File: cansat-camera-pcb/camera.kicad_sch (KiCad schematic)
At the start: 22 parts, among them IC1 TLV74315PDBVR, J3 OV5640, U1 TLV74328PDBVR

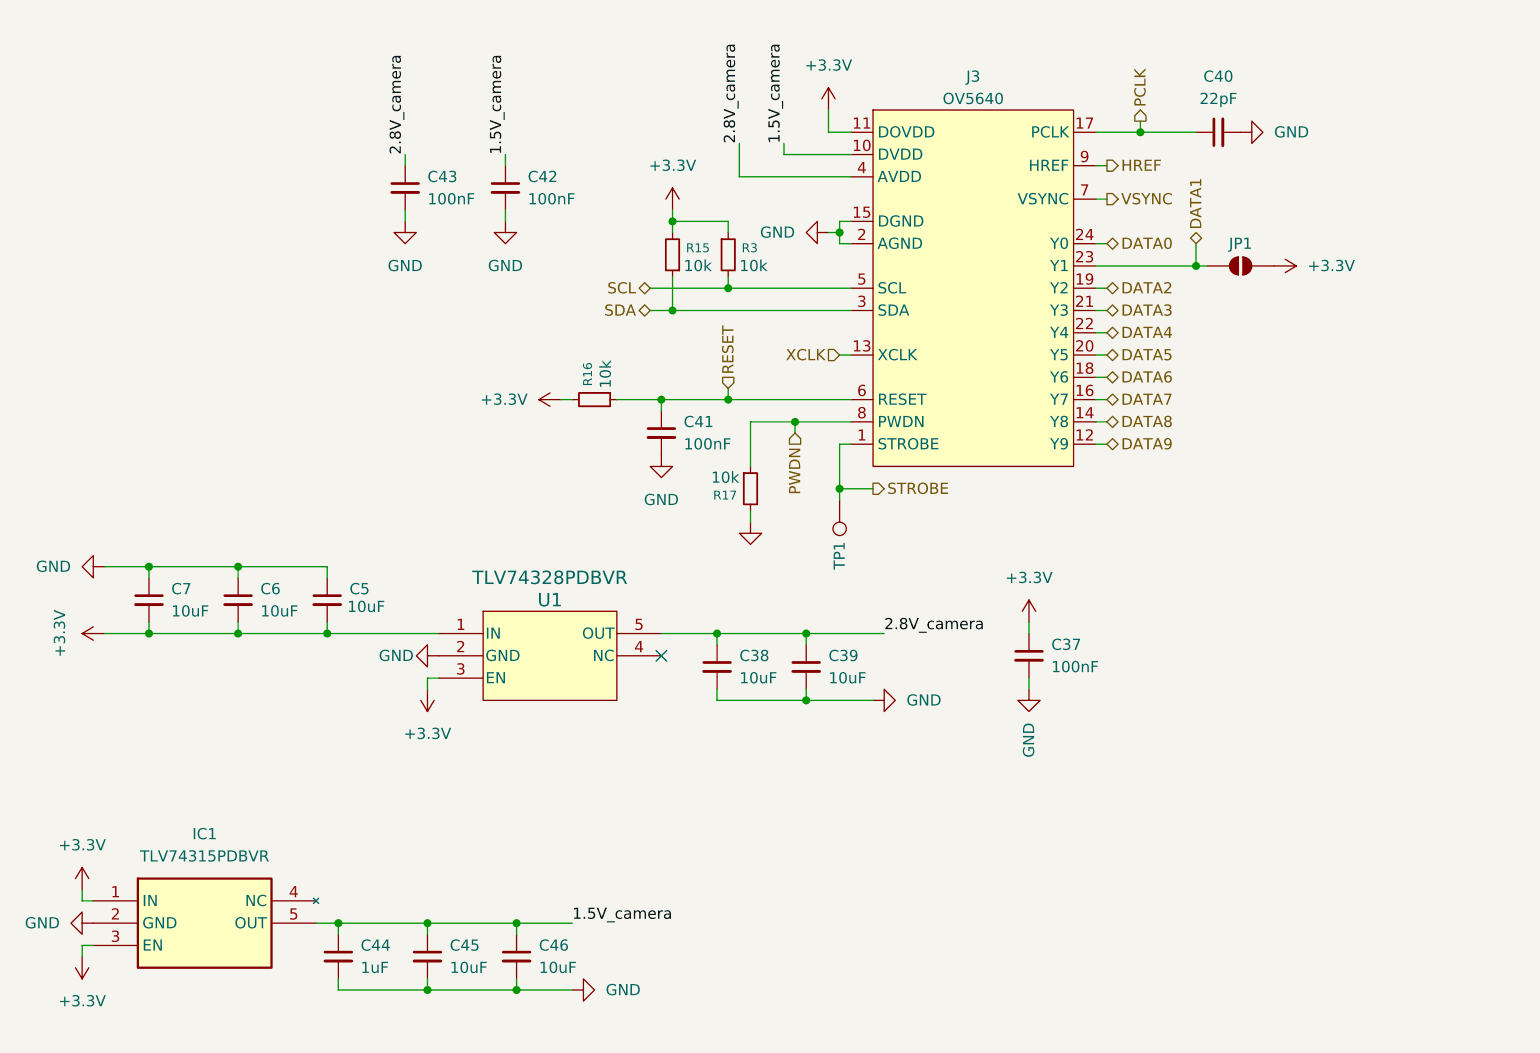
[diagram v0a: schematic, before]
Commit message: -4g modul(4g modul on other pcb)
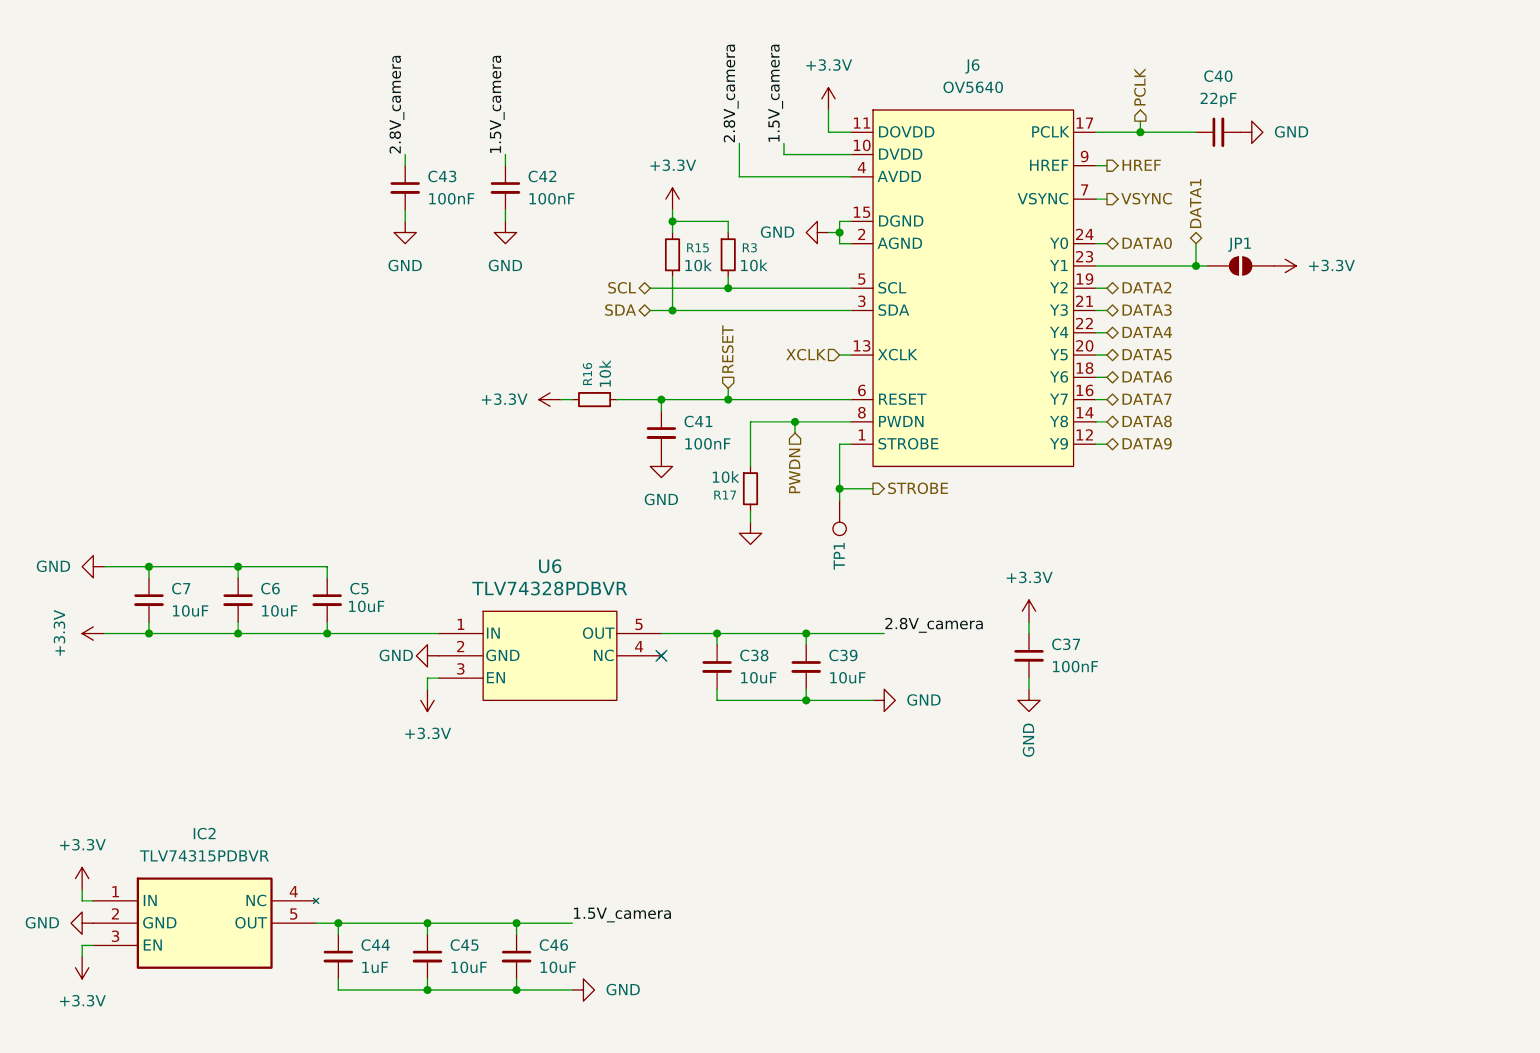
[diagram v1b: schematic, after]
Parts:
- removed IC1: TLV74315PDBVR, SOT95P280X145-5N, symbol cansat-camera-pcb-symbols:TLV74315PDBVR
- removed J3: OV5640, symbol cansat-camera-pcb-symbols:OV2640
- removed U1: TLV74328PDBVR, DBV0005A_N, symbol cansat-camera-pcb-symbols:TLV74328PDBVR
- added IC2: TLV74315PDBVR, SOT95P280X145-5N, symbol gaia-camera-symbols:TLV74315PDBVR
- added J6: OV5640, symbol gaia-camera-symbols:OV2640
- added U6: TLV74328PDBVR, DBV0005A_N, symbol gaia-camera-symbols:TLV74328PDBVR
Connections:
- net +3.3V: now also IC2.1 (IN), IC2.3 (EN), J6.11 (DOVDD), U6.1 (IN), U6.3 (EN)
- net 1.5V_camera: now also IC2.5 (OUT), J6.10 (DVDD)
- net 2.8V_camera: now also J6.4 (AVDD), U6.5 (OUT)
- net DATA0: now also J6.24 (Y0)
- net DATA1: now also J6.23 (Y1)
- net DATA2: now also J6.19 (Y2)
- net DATA3: now also J6.21 (Y3)
- net DATA4: now also J6.22 (Y4)
- net DATA5: now also J6.20 (Y5)
- net DATA6: now also J6.18 (Y6)
- net DATA7: now also J6.16 (Y7)
- net DATA8: now also J6.14 (Y8)
- net DATA9: now also J6.12 (Y9)
- net GND: now also IC2.2 (GND), J6.15 (DGND), J6.2 (AGND), U6.2 (GND)
- net HREF: now also J6.9 (HREF)
- net PCLK: now also J6.17 (PCLK)
- net PWDN: now also J6.8 (PWDN)
- net RESET: now also J6.6 (RESET)
- net SCL: now also J6.5 (SCL)
- net SDA: now also J6.3 (SDA)
- net STROBE: now also J6.1 (STROBE)
- net VSYNC: now also J6.7 (VSYNC)
- net XCLK: now also J6.13 (XCLK)

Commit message: -
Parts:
- IC2: footprint SOT95P280X145-5N -> gaia-camera-footprints:TLV74315PDBVR
- U6: footprint DBV0005A_N -> gaia-camera-footprints:TLV74328PDBVR
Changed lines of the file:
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@@
 			)
 		)
-		(property "Footprint" "SOT95P280X145-5N"
+		(property "Footprint" "gaia-camera-footprints:TLV74315PDBVR"
 			(at 43.18 213.03 0)
 			(effects
@@
 			)
 		)
-		(property "Footprint" "DBV0005A_N"
+		(property "Footprint" "gaia-camera-footprints:TLV74328PDBVR"
 			(at 73.66 90.17 0)
 			(effects

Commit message: Footprint assign
Reset kivételével minden hozzácsatolva
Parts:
- C37, C40, C41, C42, C43, R15, R16, R17, R3: footprint (none) -> Capacitor_SMD:C_0402_1005Metric
- C38, C39, C44, C45, C46, C5, C6, C7: footprint (none) -> Capacitor_SMD:C_0201_0603Metric
- J6: footprint (none) -> gaia-camera-footprints:OV5640
- JP1: footprint (none) -> Jumper:SolderJumper-2_P1.3mm_Bridged2Bar_Pad1.0x1.5mm
- TP1: footprint (none) -> TestPoint:TestPoint_Pad_2.0x2.0mm
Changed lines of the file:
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@@
 			)
 		)
-		(property "Footprint" ""
+		(property "Footprint" "Capacitor_SMD:C_0402_1005Metric"
 			(at 57.15 36.83 0)
 			(effects
@@
 			)
 		)
-		(property "Footprint" ""
+		(property "Footprint" "Jumper:SolderJumper-2_P1.3mm_Bridged2Bar_Pad1.0x1.5mm"
 			(at 152.4 45.72 0)
 			(effects
@@
 			)
 		)
-		(property "Footprint" ""
+		(property "Footprint" "Capacitor_SMD:C_0201_0603Metric"
 			(at 38.1 83.82 0)
 			(effects
@@
 			)
 		)
-		(property "Footprint" ""
+		(property "Footprint" "Capacitor_SMD:C_0402_1005Metric"
 			(at 128.27 90.17 0)
 			(effects
@@
 			)
 		)
-		(property "Footprint" ""
+		(property "Footprint" "Capacitor_SMD:C_0402_1005Metric"
 			(at 86.36 64.77 0)
 			(effects
@@
 			)
 		)
-		(property "Footprint" ""
+		(property "Footprint" "Capacitor_SMD:C_0402_1005Metric"
 			(at 68.58 36.83 0)
 			(effects
@@
 			)
 		)
-		(property "Footprint" ""
+		(property "Footprint" "Capacitor_SMD:C_0402_1005Metric"
 			(at 93.98 44.45 0)
 			(effects
@@
 			)
 		)
-		(property "Footprint" ""
+		(property "Footprint" "Capacitor_SMD:C_0402_1005Metric"
 			(at 149.86 30.48 0)
 			(effects
@@
 			)
 		)
-		(property "Footprint" ""
+		(property "Footprint" "Capacitor_SMD:C_0402_1005Metric"
 			(at 78.74 60.96 0)
 			(effects
@@
 			)
 		)
-		(property "Footprint" ""
+		(property "Footprint" "Capacitor_SMD:C_0402_1005Metric"
 			(at 87.63 44.45 0)
 			(effects
@@
 			)
 		)
-		(property "Footprint" ""
+		(property "Footprint" "Capacitor_SMD:C_0201_0603Metric"
 			(at 92.71 91.44 0)
 			(effects
@@
 			)
 		)
-		(property "Footprint" ""
+		(property "Footprint" "Capacitor_SMD:C_0201_0603Metric"
 			(at 27.94 83.82 0)
 			(effects
@@
 			)
 		)
-		(property "Footprint" ""
+		(property "Footprint" "Capacitor_SMD:C_0201_0603Metric"
 			(at 69.85 124.46 0)
 			(effects
@@
 			)
 		)
-		(property "Footprint" ""
+		(property "Footprint" "Capacitor_SMD:C_0201_0603Metric"
 			(at 49.53 124.46 0)
 			(effects
@@
 			)
 		)
-		(property "Footprint" ""
+		(property "Footprint" "Capacitor_SMD:C_0201_0603Metric"
 			(at 48.26 83.82 0)
 			(effects
@@
 			)
 		)
-		(property "Footprint" ""
+		(property "Footprint" "Capacitor_SMD:C_0201_0603Metric"
 			(at 59.69 124.46 0)
 			(effects
@@
 			)
 		)
-		(property "Footprint" ""
+		(property "Footprint" "TestPoint:TestPoint_Pad_2.0x2.0mm"
 			(at 101.6 72.39 0)
 			(effects
@@
 			)
 		)
-		(property "Footprint" ""
+		(property "Footprint" "gaia-camera-footprints:OV5640"
 			(at 121.92 49.53 0)
 			(effects
@@
 			)
 		)
-		(property "Footprint" ""
+		(property "Footprint" "Capacitor_SMD:C_0402_1005Metric"
 			(at 96.52 71.12 0)
 			(effects
@@
 			)
 		)
-		(property "Footprint" ""
+		(property "Footprint" "Capacitor_SMD:C_0201_0603Metric"
 			(at 102.87 91.44 0)
 			(effects

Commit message: Footprint assign final
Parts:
- C38, C39, C44, C45, C46, C5, C6, C7: footprint Capacitor_SMD:C_0201_0603Metric -> Capacitor_SMD:C_0603_1608Metric
- JP1: footprint Jumper:SolderJumper-2_P1.3mm_Bridged2Bar_Pad1.0x1.5mm -> Jumper:SolderJumper-2_P1.3mm_Open_Pad1.0x1.5mm
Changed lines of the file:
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@@
 			)
 		)
-		(property "Footprint" "Jumper:SolderJumper-2_P1.3mm_Bridged2Bar_Pad1.0x1.5mm"
+		(property "Footprint" "Jumper:SolderJumper-2_P1.3mm_Open_Pad1.0x1.5mm"
 			(at 152.4 45.72 0)
 			(effects
@@
 			)
 		)
-		(property "Footprint" "Capacitor_SMD:C_0201_0603Metric"
+		(property "Footprint" "Capacitor_SMD:C_0603_1608Metric"
 			(at 38.1 83.82 0)
 			(effects
@@
 			)
 		)
-		(property "Footprint" "Capacitor_SMD:C_0201_0603Metric"
+		(property "Footprint" "Capacitor_SMD:C_0603_1608Metric"
 			(at 92.71 91.44 0)
 			(effects
@@
 			)
 		)
-		(property "Footprint" "Capacitor_SMD:C_0201_0603Metric"
+		(property "Footprint" "Capacitor_SMD:C_0603_1608Metric"
 			(at 27.94 83.82 0)
 			(effects
@@
 			)
 		)
-		(property "Footprint" "Capacitor_SMD:C_0201_0603Metric"
+		(property "Footprint" "Capacitor_SMD:C_0603_1608Metric"
 			(at 69.85 124.46 0)
 			(effects
@@
 			)
 		)
-		(property "Footprint" "Capacitor_SMD:C_0201_0603Metric"
+		(property "Footprint" "Capacitor_SMD:C_0603_1608Metric"
 			(at 49.53 124.46 0)
 			(effects
@@
 			)
 		)
-		(property "Footprint" "Capacitor_SMD:C_0201_0603Metric"
+		(property "Footprint" "Capacitor_SMD:C_0603_1608Metric"
 			(at 48.26 83.82 0)
 			(effects
@@
 			)
 		)
-		(property "Footprint" "Capacitor_SMD:C_0201_0603Metric"
+		(property "Footprint" "Capacitor_SMD:C_0603_1608Metric"
 			(at 59.69 124.46 0)
 			(effects
@@
 			)
 		)
-		(property "Footprint" "Capacitor_SMD:C_0201_0603Metric"
+		(property "Footprint" "Capacitor_SMD:C_0603_1608Metric"
 			(at 102.87 91.44 0)
 			(effects

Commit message: Alkatrész elhelyezés final
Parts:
- removed C37: 100nF, Capacitor_SMD:C_0402_1005Metric, symbol Device:C_Small
- removed C39, C45, C46, C7: 10uF, Capacitor_SMD:C_0603_1608Metric, symbol Device:C_Small
- C38, C5, C6: value 10uF -> 1uF
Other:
- moved on the sheet: C44, C5, IC2

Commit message: ready
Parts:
- R15, R16, R17, R3: footprint Capacitor_SMD:C_0402_1005Metric -> Resistor_SMD:R_0402_1005Metric
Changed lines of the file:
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@@
 			)
 		)
-		(property "Footprint" "Capacitor_SMD:C_0402_1005Metric"
+		(property "Footprint" "Resistor_SMD:R_0402_1005Metric"
 			(at 93.98 44.45 0)
 			(effects
@@
 			)
 		)
-		(property "Footprint" "Capacitor_SMD:C_0402_1005Metric"
+		(property "Footprint" "Resistor_SMD:R_0402_1005Metric"
 			(at 78.74 60.96 0)
 			(effects
@@
 			)
 		)
-		(property "Footprint" "Capacitor_SMD:C_0402_1005Metric"
+		(property "Footprint" "Resistor_SMD:R_0402_1005Metric"
 			(at 87.63 44.45 0)
 			(effects
@@
 			)
 		)
-		(property "Footprint" "Capacitor_SMD:C_0402_1005Metric"
+		(property "Footprint" "Resistor_SMD:R_0402_1005Metric"
 			(at 96.52 71.12 0)
 			(effects

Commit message: some fixes
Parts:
- added Y2: ECS-2520MVQ-240-BS-TR, ECS2520MVQ240BSTR, symbol gaia-camera-symbols:ECS-2520MVQ-240-BS-TR
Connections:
- net +3.3V: now also Y2.1 (TRI-STATE), Y2.4 (VDD)
- net GND: now also Y2.2 (GND)
- net XCLK: now also Y2.3 (OUTPUT)

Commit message: Regulator+
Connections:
- net +3.3V renamed +3.3VA
